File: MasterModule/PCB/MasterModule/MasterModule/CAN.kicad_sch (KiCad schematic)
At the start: 8 parts, among them J1 Input_7V, U1 AMS1117-3.3, U2 AMS1117-5.0

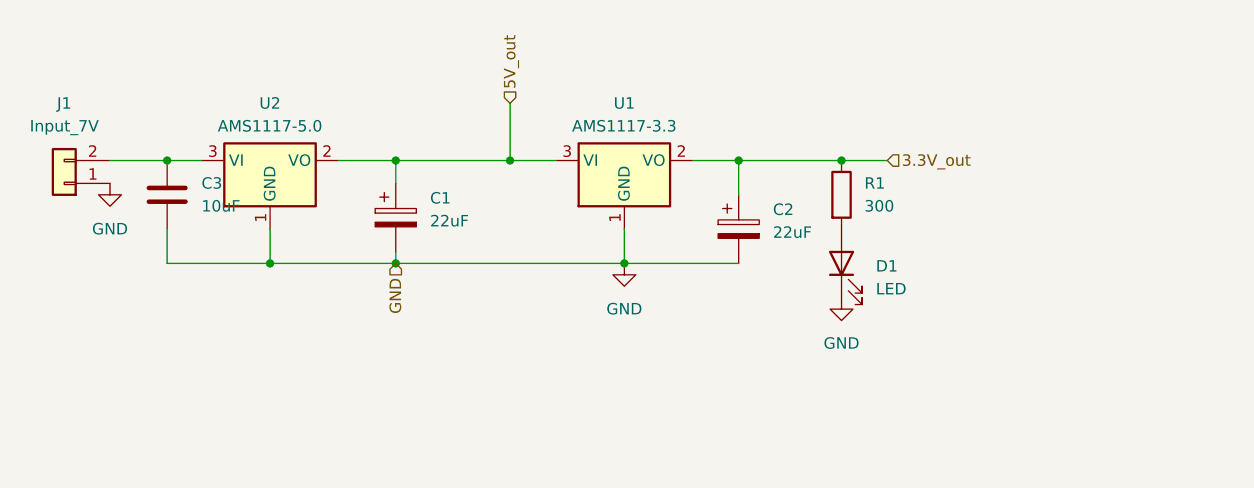
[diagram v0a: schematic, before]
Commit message: [PCB][MasterModule] Create MasterModule v.1.0
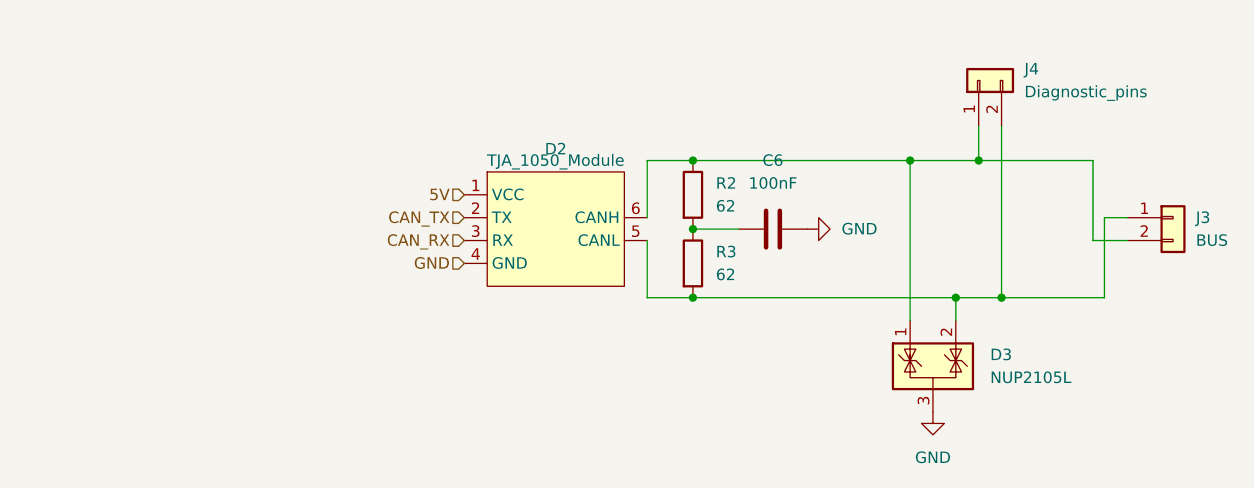
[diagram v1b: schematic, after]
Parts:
- removed C1, C2: 22uF, Capacitor_SMD:C_1210_3225Metric_Pad1.33x2.70mm_HandSolder, symbol Device:C_Polarized
- removed C3: 10uF, Capacitor_SMD:C_0805_2012Metric_Pad1.18x1.45mm_HandSolder, symbol Device:C
- removed D1: LED, LED_SMD:LED_0805_2012Metric_Pad1.15x1.40mm_HandSolder, symbol Device:LED
- removed J1: Input_7V, TerminalBlock_Phoenix:TerminalBlock_Phoenix_MKDS-1,5-2-5.08_1x02_P5.08mm_Horizontal, symbol Connector_Generic:Conn_01x02
- removed R1: 300, Resistor_SMD:R_0805_2012Metric_Pad1.20x1.40mm_HandSolder, symbol Device:R
- removed U1: AMS1117-3.3, Package_TO_SOT_SMD:SOT-223-3_TabPin2, symbol Regulator_Linear:AMS1117-3.3
- removed U2: AMS1117-5.0, Package_TO_SOT_SMD:SOT-223-3_TabPin2, symbol Regulator_Linear:AMS1117-5.0
- added C6: 100nF, Capacitor_SMD:C_0805_2012Metric_Pad1.18x1.45mm_HandSolder, symbol Device:C
- added D2: TJA_1050_Module, MasterModuleCANFootprint:TJA1050_module, symbol MasterModuleCAN:TJA1050_CAN_Module
- added D3: NUP2105L, Package_TO_SOT_SMD:SOT-23, symbol Power_Protection:NUP2105L
- added J3: BUS, Connector_JST:JST_XH_B2B-XH-A_1x02_P2.50mm_Vertical, symbol Connector_Generic:Conn_01x02
- added J4: Diagnostic_pins, Connector_PinSocket_2.54mm:PinSocket_1x02_P2.54mm_Vertical, symbol Connector_Generic:Conn_01x02
- added R2, R3: 62, Resistor_SMD:R_0805_2012Metric_Pad1.20x1.40mm_HandSolder, symbol Device:R
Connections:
- net GND: now also C6.2, D2.4 (GND), D3.3 (A)
- new net: D2.6 (CANH), D3.1 (K), J3.2 (Pin_2), J4.1 (Pin_1), R2.1
- new net: D2.5 (CANL), D3.2 (K), J3.1 (Pin_1), J4.2 (Pin_2), R3.2
- new net: C6.1, R2.2, R3.1
- new net 5V: D2.1 (VCC)
- new net CAN_RX: D2.3 (RX)
- new net CAN_TX: D2.2 (TX)

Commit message: [PCB][MasterModule] Fix CAN transmitter to TJA1050 chip (Master v1.1)
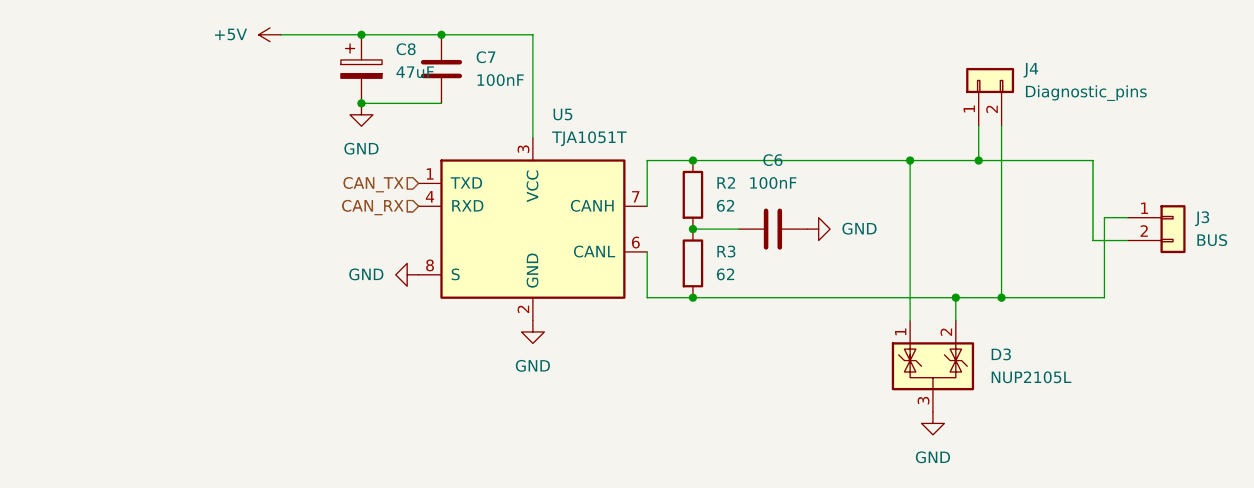
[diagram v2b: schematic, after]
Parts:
- removed D2: TJA_1050_Module, MasterModuleCANFootprint:TJA1050_module, symbol MasterModuleCAN:TJA1050_CAN_Module
- added C7: 100nF, Capacitor_SMD:C_0603_1608Metric_Pad1.08x0.95mm_HandSolder, symbol Device:C
- added C8: 47uF, Capacitor_SMD:C_1210_3225Metric_Pad1.33x2.70mm_HandSolder, symbol Device:C_Polarized
- added U5: TJA1051T, Package_SO:SOIC-8_3.9x4.9mm_P1.27mm, symbol Interface_CAN_LIN:TJA1051T
- C6: footprint Capacitor_SMD:C_0805_2012Metric_Pad1.18x1.45mm_HandSolder -> Capacitor_SMD:C_0603_1608Metric_Pad1.08x0.95mm_HandSolder
- R2, R3: footprint Resistor_SMD:R_0805_2012Metric_Pad1.20x1.40mm_HandSolder -> Resistor_SMD:R_1206_3216Metric
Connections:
- net CAN_RX: now also U5.4 (RXD)
- net CAN_TX: now also U5.1 (TXD)
- net GND: now also C7.2, C8.2, U5.2 (GND), U5.8 (S)
- net at D3.1 (K), J3.2 (Pin_2), J4.1 (Pin_1)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: now also U5.7 (CANH)
- net at D3.2 (K), J3.1 (Pin_1), J4.2 (Pin_2)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: now also U5.6 (CANL)
- new net +5V: C7.1, C8.1, U5.3 (VCC)
